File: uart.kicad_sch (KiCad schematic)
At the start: 45 parts, among them J17 USB_B, J18 D09P33E4GV00LF, J19 D09P33E4GV00LF, U17 TS5A23159DGS, U18 CP2104, U19 TRS3221ECPW, U20 TRS3221ECPW

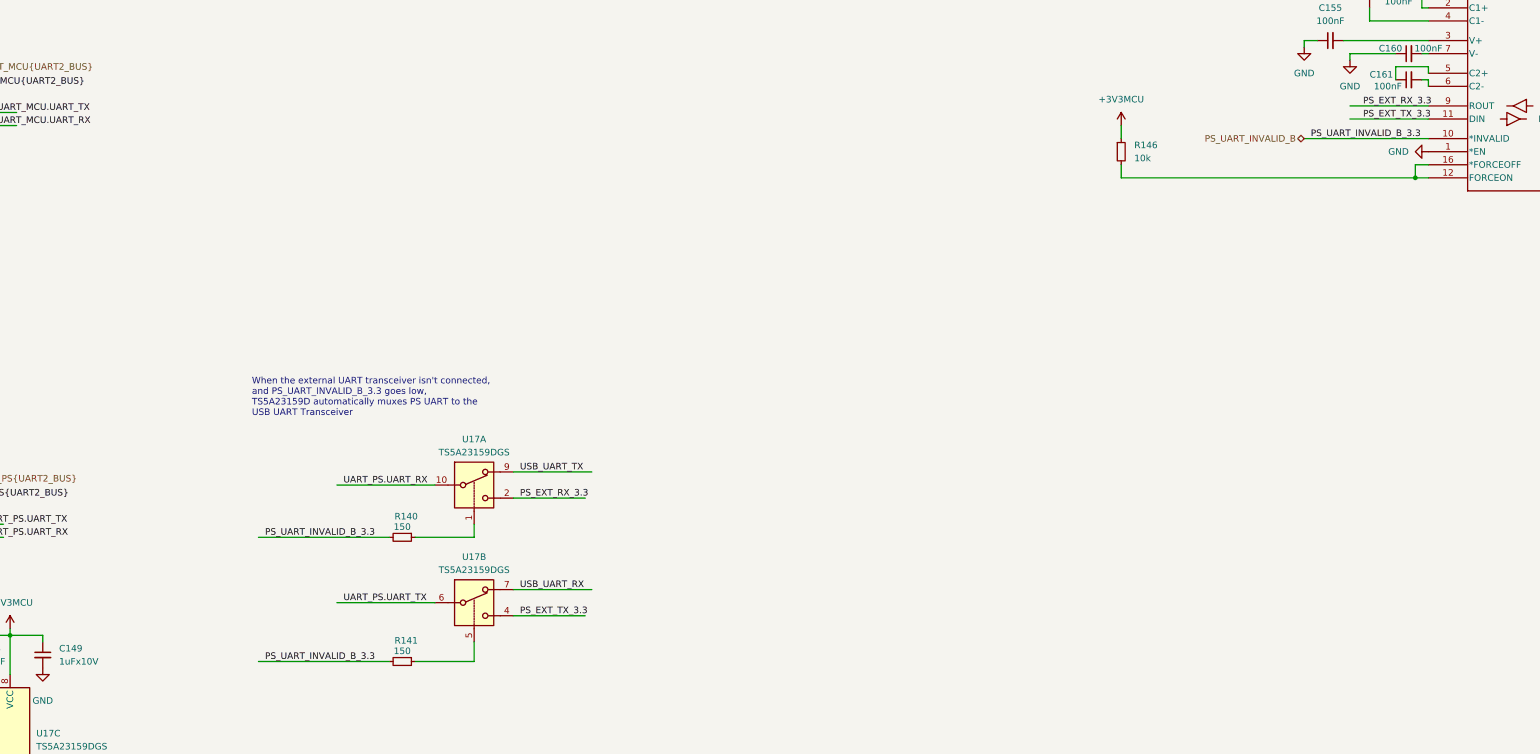
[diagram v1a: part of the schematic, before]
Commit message: schema: AC term of SOC primary clock
AC term of primary 33.333 clock
ERRATA updates
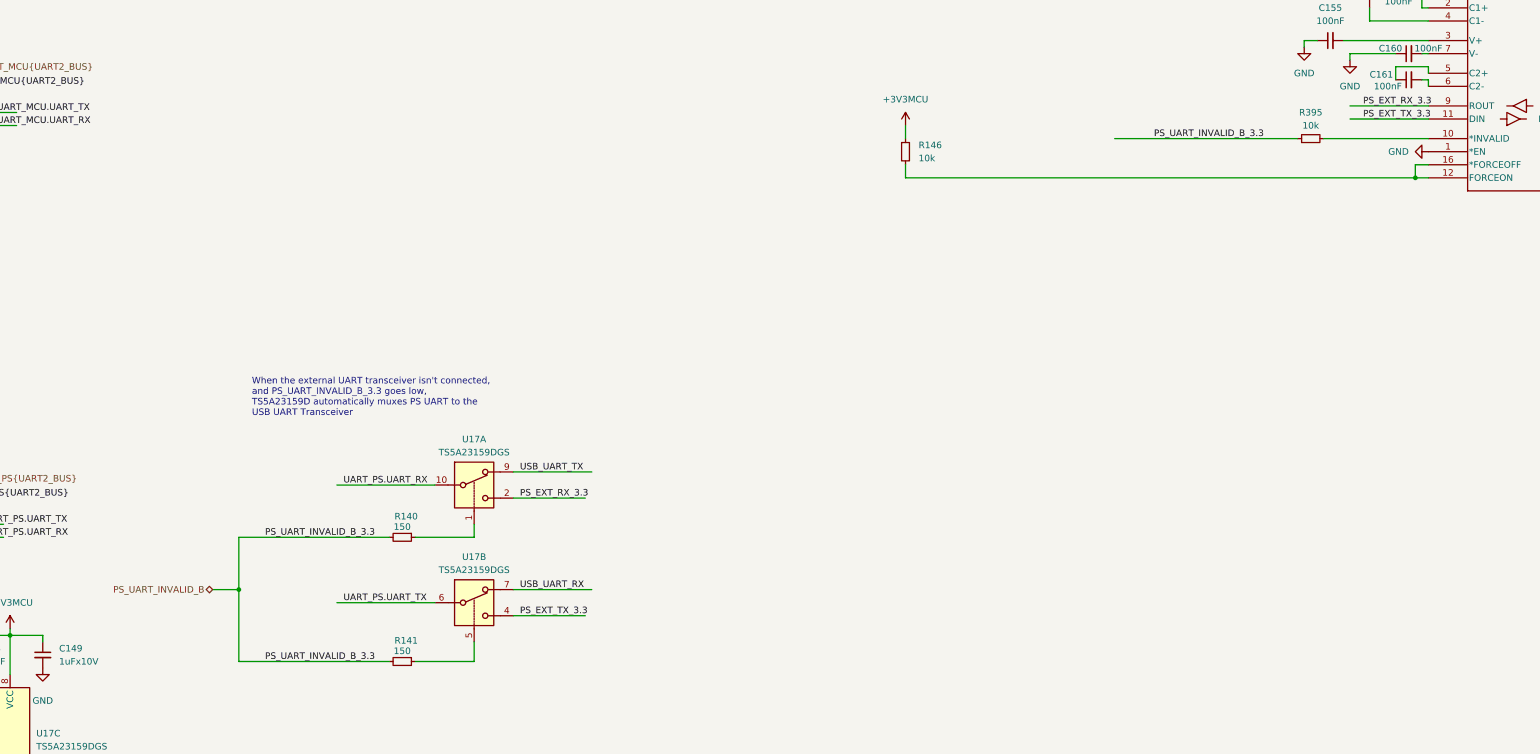
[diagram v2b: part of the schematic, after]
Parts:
- added R395: 10k, Resistor_SMD:R_0402_1005Metric, symbol Device:R_Small
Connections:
- net PS_UART_INVALID_B: now also R395.1; no longer U20.10 (*INVALID)
- new net: R395.2, U20.10 (*INVALID)
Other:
- moved on the sheet: R146
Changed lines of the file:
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@@
 	)
 	(junction
+		(at 78.74 229.87)
+		(diameter 0)
+		(color 0 0 0 0)
+	)
+	(junction
 		(at 307.34 73.66)
 		(diameter 0)
@@
 	(wire
 		(pts
+			(xy 78.74 219.71) (xy 107.95 219.71)
+		)
+		(stroke
+			(width 0)
+			(type default)
+		)
+	)
+	(wire
+		(pts
 			(xy 345.44 73.66) (xy 345.44 74.93)
 		)
@@
 	(wire
 		(pts
-			(xy 82.55 219.71) (xy 107.95 219.71)
+			(xy 298.45 33.02) (xy 298.45 35.56)
 		)
 		(stroke
@@
 	(wire
 		(pts
-			(xy 298.45 33.02) (xy 298.45 35.56)
+			(xy 100.33 50.8) (xy 118.11 50.8)
 		)
 		(stroke
@@
 	(wire
 		(pts
-			(xy 100.33 50.8) (xy 118.11 50.8)
+			(xy 66.04 63.5) (xy 74.93 63.5)
 		)
 		(stroke
@@
 	(wire
 		(pts
-			(xy 66.04 63.5) (xy 74.93 63.5)
+			(xy 309.88 54.61) (xy 309.88 55.88)
 		)
 		(stroke
@@
 	(wire
 		(pts
-			(xy 309.88 54.61) (xy 309.88 55.88)
+			(xy 78.74 229.87) (xy 78.74 243.84)
 		)
 		(stroke
@@
 	(wire
 		(pts
-			(xy 82.55 243.84) (xy 107.95 243.84)
-		)
-		(stroke
-			(width 0)
-			(type default)
-		)
-	)
-	(wire
-		(pts
 			(xy 345.44 40.64) (xy 344.17 40.64)
 		)
@@
 	(wire
 		(pts
-			(xy 285.75 142.24) (xy 309.88 142.24)
+			(xy 248.92 142.24) (xy 284.48 142.24)
 		)
 		(stroke
@@
 	(wire
 		(pts
+			(xy 78.74 243.84) (xy 107.95 243.84)
+		)
+		(stroke
+			(width 0)
+			(type default)
+		)
+	)
+	(wire
+		(pts
 			(xy 294.64 138.43) (xy 309.88 138.43)
 		)
@@
 	(wire
 		(pts
-			(xy 250.19 139.7) (xy 250.19 142.24)
+			(xy 208.28 139.7) (xy 208.28 142.24)
 		)
 		(stroke
@@
 	(wire
 		(pts
-			(xy 250.19 149.86) (xy 307.34 149.86)
+			(xy 208.28 149.86) (xy 307.34 149.86)
 		)
 		(stroke
@@
 	(wire
 		(pts
-			(xy 250.19 147.32) (xy 250.19 149.86)
+			(xy 208.28 147.32) (xy 208.28 149.86)
 		)
 		(stroke
@@
 	(wire
 		(pts
+			(xy 78.74 219.71) (xy 78.74 229.87)
+		)
+		(stroke
+			(width 0)
+			(type default)
+		)
+	)
+	(wire
+		(pts
 			(xy 100.33 48.26) (xy 105.41 48.26)
 		)
@@
 	(wire
 		(pts
+			(xy 73.66 229.87) (xy 78.74 229.87)
+		)
+		(stroke
+			(width 0)
+			(type default)
+		)
+	)
+	(wire
+		(pts
 			(xy 308.61 125.73) (xy 309.88 125.73)
 		)
@@
 	(wire
 		(pts
+			(xy 289.56 142.24) (xy 309.88 142.24)
+		)
+		(stroke
+			(width 0)
+			(type default)
+		)
+	)
+	(wire
+		(pts
 			(xy 43.18 68.58) (xy 46.99 68.58)
 		)
@@
 	)
 	(label "PS_UART_INVALID_B_3.3"
-		(at 287.02 142.24 0)
+		(at 256.54 142.24 0)
 		(effects
 			(font
@@
 		)
 	)
-	(hierarchical_label "UART_MCU{UART2_BUS}"
+	(hierarchical_label "PS_UART_INVALID_B"
 		(shape bidirectional)
-		(at 26.67 128.27 0)
+		(at 73.66 229.87 180)
 		(effects
 			(font
 				(size 1.27 1.27)
 			)
-			(justify left)
+			(justify right)
 		)
 	)
-	(hierarchical_label "MCU_UART_INVALID_B"
-		(shape output)
-		(at 287.02 66.04 180)
+	(hierarchical_label "UART_MCU{UART2_BUS}"
+		(shape bidirectional)
+		(at 26.67 128.27 0)
 		(effects
 			(font
 				(size 1.27 1.27)
 			)
-			(justify right)
+			(justify left)
 		)
 	)
-	(hierarchical_label "PS_UART_INVALID_B"
-		(shape bidirectional)
-		(at 285.75 142.24 180)
+	(hierarchical_label "MCU_UART_INVALID_B"
+		(shape output)
+		(at 287.02 66.04 180)
 		(effects
 			(font
@@
 	(symbol
 		(lib_id "Device:R_Small")
-		(at 250.19 144.78 0)
+		(at 208.28 144.78 0)
 		(unit 1)
 		(exclude_from_sim no)
@@
 		(fields_autoplaced yes)
 		(property "Reference" "R146"
-			(at 252.73 143.5099 0)
+			(at 210.82 143.5099 0)
 			(effects
 				(font
@@
 		)
 		(property "Value" "10k"
-			(at 252.73 146.0499 0)
+			(at 210.82 146.0499 0)
 			(effects
 				(font
@@
 		)
 		(property "Footprint" "Resistor_SMD:R_0402_1005Metric"
-			(at 250.19 144.78 0)
+			(at 208.28 144.78 0)
 			(effects
 				(font
@@
 		)
 		(property "Datasheet" "~"
-			(at 250.19 144.78 0)
+			(at 208.28 144.78 0)
 			(effects
 				(font
@@
 		)
 		(property "Description" ""
-			(at 250.19 144.78 0)
+			(at 208.28 144.78 0)
 			(effects
 				(font
@@
 		)
 		(property "JLCPCB Part #" "C25744"
-			(at 250.19 144.78 0)
+			(at 208.28 144.78 0)
 			(effects
 				(font
@@
 		)
 		(property "Part" "0402WGF1002TCE"
-			(at 250.19 144.78 0)
+			(at 208.28 144.78 0)
 			(effects
 				(font
@@
 		)
 		(property "Mouser " ""
-			(at 250.19 144.78 0)
+			(at 208.28 144.78 0)
 			(effects
 				(font
@@
 	(symbol
 		(lib_id "GPWR3V3MCU:+3V3MCU")
-		(at 250.19 139.7 0)
+		(at 208.28 139.7 0)
 		(unit 1)
 		(exclude_from_sim no)
@@
 		(fields_autoplaced yes)
 		(property "Reference" "#PWR3V3MCU047"
-			(at 250.19 143.51 0)
+			(at 208.28 143.51 0)
 			(effects
 				(font
@@
 		)
 		(property "Value" "+3V3MCU"
-			(at 250.19 134.62 0)
+			(at 208.28 134.62 0)
 			(effects
 				(font
@@
 		)
 		(property "Footprint" ""
-			(at 250.19 139.7 0)
+			(at 208.28 139.7 0)
 			(effects
 				(font
@@
 		)
 		(property "Datasheet" ""
-			(at 250.19 139.7 0)
+			(at 208.28 139.7 0)
 			(effects
 				(font
@@
 		)
 		(property "Description" ""
-			(at 250.19 139.7 0)
+			(at 208.28 139.7 0)
 			(effects
 				(font
@@
 					(unit 1)
 				)
+			)
+		)
+	)
+	(symbol
+		(lib_id "Device:R_Small")
+		(at 287.02 142.24 90)
+		(unit 1)
+		(exclude_from_sim no)
+		(in_bom yes)
+		(on_board yes)
+		(dnp no)
+		(fields_autoplaced yes)
+		(property "Reference" "R395"
+			(at 287.02 137.16 90)
+			(effects
+				(font
+					(size 1.27 1.27)
+				)
+			)
+		)
+		(property "Value" "10k"
+			(at 287.02 139.7 90)
+			(effects
+				(font
+					(size 1.27 1.27)
+				)
+			)
+		)
+		(property "Footprint" "Resistor_SMD:R_0402_1005Metric"
+			(at 287.02 142.24 0)
+			(effects
+				(font
+					(size 1.27 1.27)
+				)
+				(hide yes)
+			)
+		)
+		(property "Datasheet" "~"
+			(at 287.02 142.24 0)
+			(effects
+				(font
+					(size 1.27 1.27)
+				)
+				(hide yes)
+			)
+		)
+		(property "Description" ""
+			(at 287.02 142.24 0)
+			(effects
+				(font
+					(size 1.27 1.27)
+				)
+				(hide yes)
+			)
+		)
+		(property "JLCPCB Part #" "C25744"
+			(at 287.02 142.24 0)
+			(effects
+				(font
+					(size 1.27 1.27)
+				)
+				(hide yes)
+			)
+		)
+		(property "Part" "0402WGF1002TCE"
+			(at 287.02 142.24 0)
+			(effects
+				(font
+					(size 1.27 1.27)
+				)
+				(hide yes)
+			)
+		)
+		(property "Mouser " ""
+			(at 287.02 142.24 0)
+			(effects
+				(font
+					(size 1.27 1.27)
+				)
+				(hide yes)
+			)
+		)
+		(pin "1"
+		)
+		(pin "2"
+		)
+		(instances
+			(project "NASR"
+				(path "/9a13c8f9-b8a2-41aa-b5bd-813f44236e01/7514f663-2447-40f5-9da9-2cca20702750"
+					(reference "R395")
+					(unit 1)
+				)
